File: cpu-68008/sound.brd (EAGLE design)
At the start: 99.7 x 99.7 mm, 36 parts, among them IC101 GAL22V10D, IC102 74HCT175N, IC201 74HC73, IC202 YM3812, IC203 YM3014B, IC204 AY-3-8910, IC301 TL062

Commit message: added analog component to mix on sound card
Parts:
- added C304, C307: 100nF, rcl:C0805
- added C305, C306: 4.7µF, rcl:E2-5
- added IC302: TL062, linear:DIL08
- added R305, R306: 1k, pot:PT-10S
- added R307, R308: 1k, rcl:R2012
- added R309, R310: 4k7, rcl:R2012
- added R311: 10k, pot:PT-10S
- C303: value 100nF -> 220µF; device rcl:C0805 -> rcl:E2,5-6
- moved C303 57.3 mm to (14.0, 91.4), flipped to the top, turned to 90 degrees
- moved R304 15.4 mm to (48.3, 55.2), turned to 0 degrees
- moved R303 15.3 mm to (52.5, 55.2), turned to 0 degrees
- moved R301 12.3 mm to (51.4, 58.4), turned to 90 degrees
- moved R302 12.3 mm to (54.0, 58.4), turned to 90 degrees
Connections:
- new net AUDIO: C303.+, IC302.1, R311.S
- new net N$1: C305.+, R305.S
- new net N$10: C305.-, R307.1
- new net N$11: C306.-, R308.1
- new net N$12: IC302.2, R307.2, R308.2, R311.A
- new net N$13: IC302.6, IC302.7
- new net N$15: IC302.5, R309.2, R310.1
- net +5V: now also C304.1, C307.1, IC302.8, R309.1; no longer C303.1
- net FM_OUT: now also R305.E
- net GND: now also C304.2, C307.2, IC302.3, IC302.4, R305.A, R306.A, R310.2; no longer C303.2
- net N$4: now also C303.-
- net N$7: now also C306.+, R306.S; no longer IC101.7
- net PSG_OUT: now also R306.E
- net SLOT_A0: now also IC101.7
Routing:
- net +5V: track 321.6 -> 379.8 mm, vias 3 -> 4
- net N$12: track 0.00 -> 38.0 mm
- net SLOT_A0: track 59.2 -> 85.9 mm
- net AUDIO: track 0.00 -> 15.7 mm
- net PSG_OUT_C: track 21.5 -> 6.89 mm
- net PSG_OUT: track 7.62 -> 22.0 mm
- net N$15: track 0.00 -> 13.9 mm
- net N$10: track 0.00 -> 9.83 mm
- net N$7: track 0.00 -> 7.87 mm
- net N$1: track 0.00 -> 7.87 mm
- net N$11: track 0.00 -> 6.02 mm
- net N$4: track 0.00 -> 5.50 mm
- net PSG_OUT_A: track 4.87 -> 7.42 mm
- net N$13: track 0.00 -> 2.54 mm
- net PSG_OUT_B: track 4.87 -> 7.30 mm
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
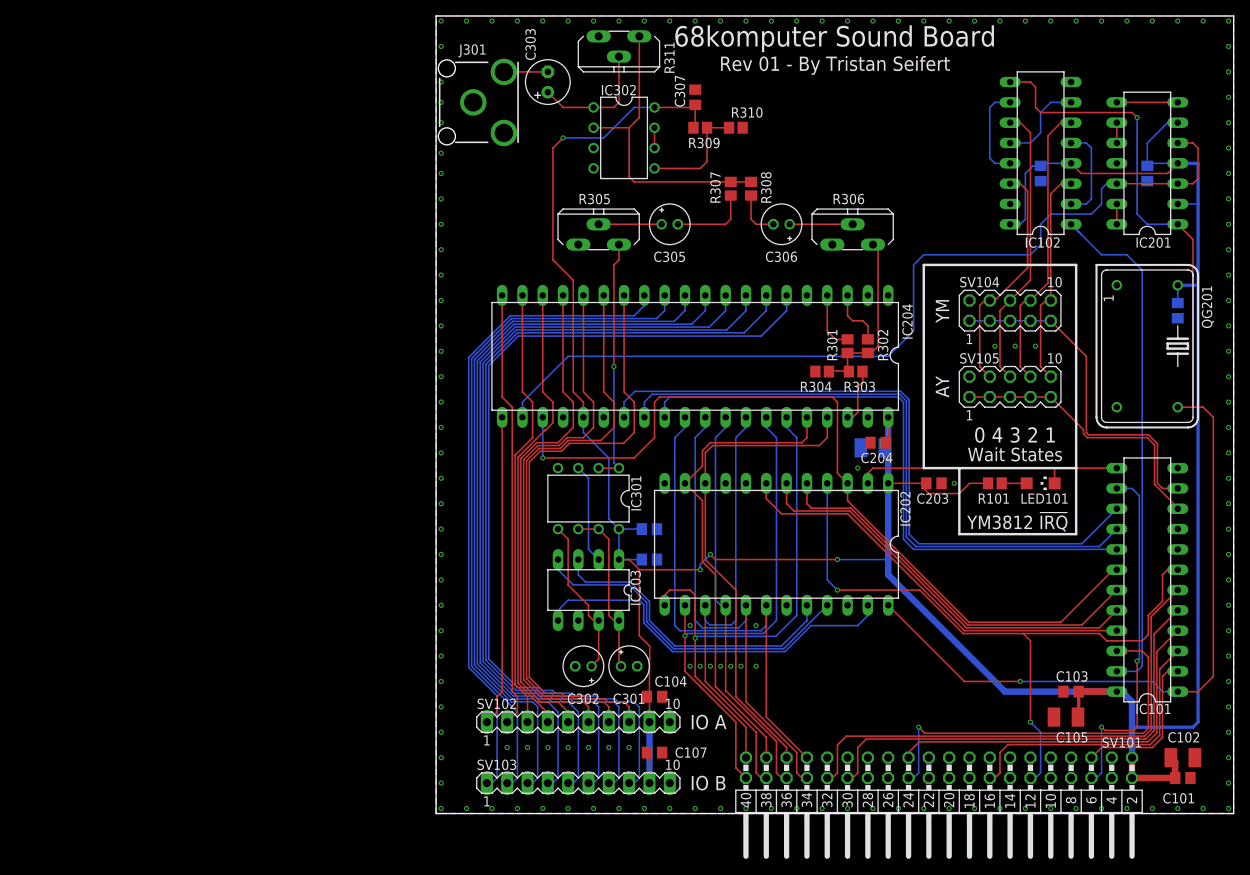
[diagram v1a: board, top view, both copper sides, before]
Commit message: start working on adding midi in/out to sound board
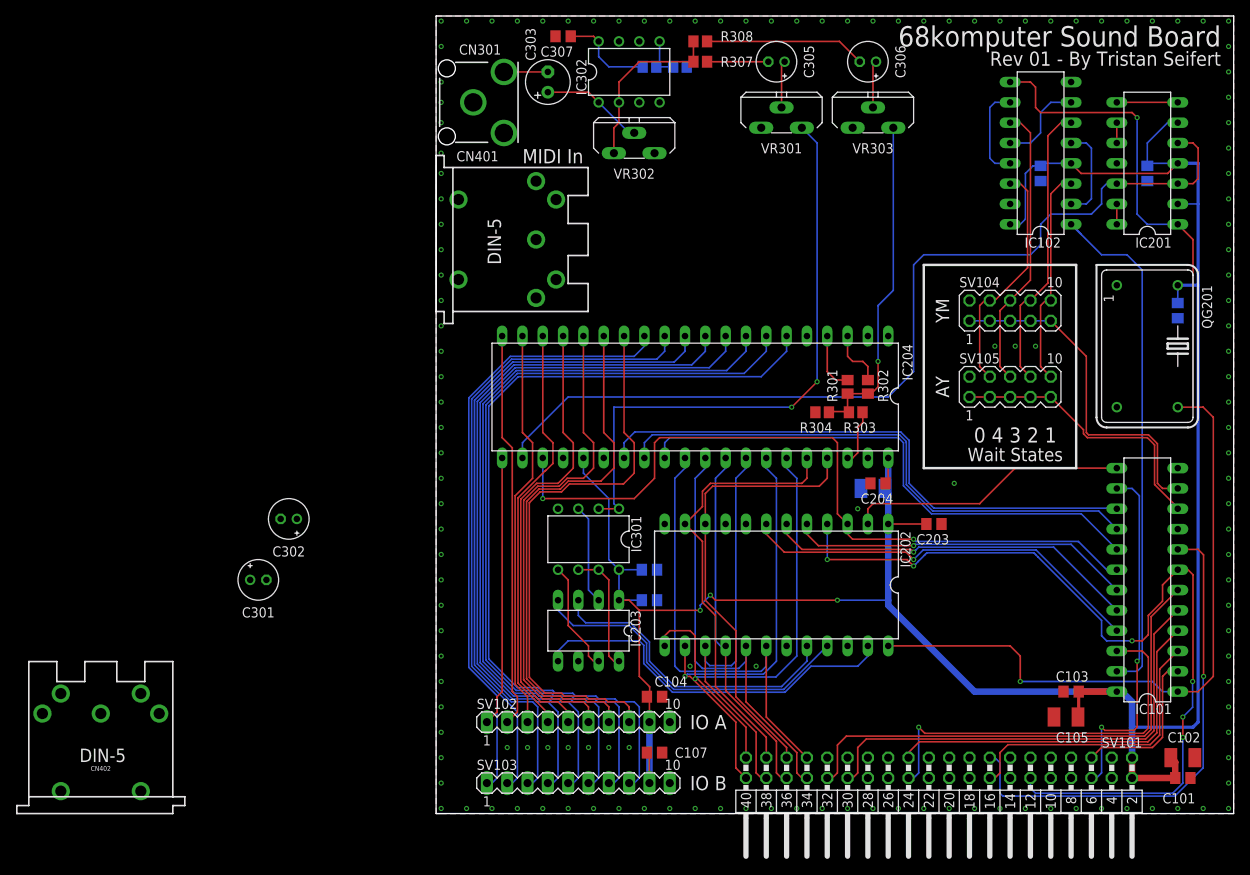
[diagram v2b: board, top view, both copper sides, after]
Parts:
- removed LED101: (no value), led:CHIPLED_1206
- removed R101: 3k, rcl:R2012
- removed R305, R306: 1k, pot:PT-10S
- removed R311: 10k, pot:PT-10S
- added CN401, CN402: DIN5, SparkFun-Connectors:DIN5-RA-PTH
- added VR301, VR303: 1k, pot:PT-10S
- added VR302: 10k, pot:PT-10S
- moved C301 47.6 mm to (-22.2, 29.2)
- moved C302 41.2 mm to (-18.4, 36.8)
- moved C305 24.3 mm to (42.5, 94.0), turned to 180 degrees
- moved C306 23.0 mm to (54.0, 94.0)
- moved R308 19.5 mm to (33.0, 96.5), turned to 180 degrees
- moved C307 18.2 mm to (15.9, 97.2), turned to 180 degrees
- moved R307 16.3 mm to (33.0, 94.0), turned to 180 degrees
- moved R310 10.3 mm to (30.5, 93.3), flipped to the bottom, turned to 180 degrees
- moved R309 9.92 mm to (26.7, 93.3), flipped to the bottom, turned to 180 degrees
- moved IC302 8.28 mm to (24.1, 92.7), turned to 0 degrees
- moved C304 5.08 mm to (26.7, 30.5)
- moved IC202 5.08 mm to (42.5, 28.6)
- moved IC203 5.08 mm to (19.1, 22.9)
- moved C203 5.08 mm to (62.2, 36.2)
- moved C204 5.08 mm to (55.2, 41.3)
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- renumbered J301 to CN301
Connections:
- removed net N$3: LED101.A, R101.2
- removed net N$8: IC101.8
- net !YM_IRQ: no longer LED101.C
- net +5V: no longer R101.1
- net AUDIO: now also VR302.S; no longer R311.S
- net FM_OUT: now also VR301.E; no longer R305.E
- net GND: now also VR301.A, VR303.A; no longer R305.A, R306.A
- net N$1: now also VR301.S; no longer R305.S
- net N$12: now also VR302.A; no longer R311.A
- net N$7: now also VR303.S; no longer R306.S
- net PSG_OUT: now also VR303.E; no longer R306.E
- net SLOT_A9: now also IC101.8
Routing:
- net +5V: track 379.8 -> 316.7 mm, vias 4 -> 3
- net SLOT_A9: track 0.00 -> 62.5 mm, vias 0 -> 1
- net FM_OUT: track 31.0 -> 74.8 mm, vias 1 -> 2
- net SLOT_A0: track 85.9 -> 111.1 mm, vias 2 -> 6
- net PSG_OUT: track 22.0 -> 42.2 mm, vias 0 -> 1
- net N$12: track 38.0 -> 22.1 mm
- net N$11: track 6.02 -> 20.1 mm
- net AY_BDIR: track 83.6 -> 71.2 mm
- net AY_BC2: track 80.1 -> 69.4 mm
- net AY_BC1: track 76.6 -> 67.6 mm
- net N$15: track 13.9 -> 5.28 mm
- net !RESET: track 103.4 -> 95.4 mm, vias 1 -> 2
- net !YM_WR: track 49.4 -> 43.0 mm, vias 0 -> 1
- net YM_OUT_RB: track 20.0 -> 13.9 mm
- net YM_OUT_MP: track 21.2 -> 15.4 mm
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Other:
- board text added: "MIDI In"
- board text removed: "YM3812 !IRQ!"

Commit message: cleaned up routing for sound board a bit, moved some things in preparation of adding midi interface
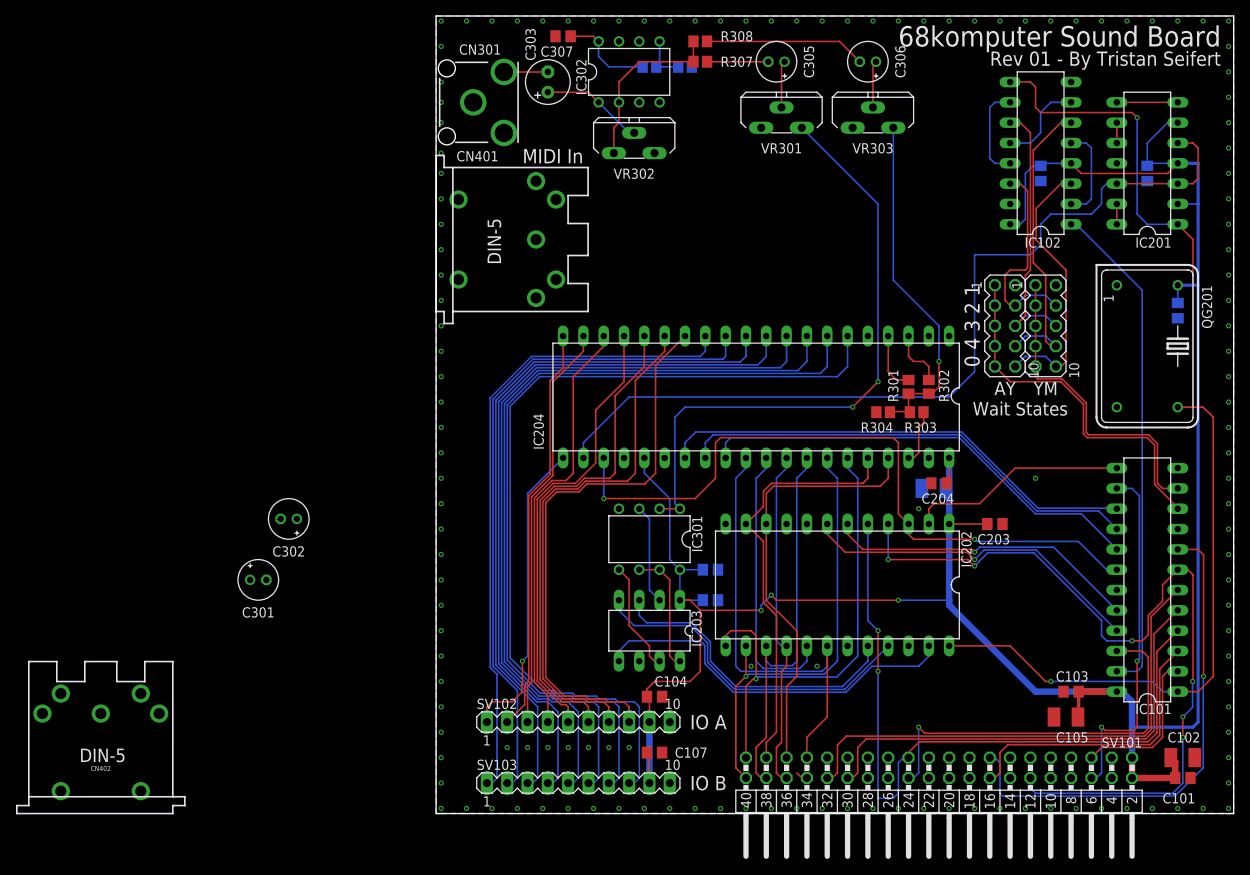
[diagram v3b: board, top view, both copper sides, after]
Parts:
- moved SV105 7.65 mm to (71.1, 61.0), turned to 270 degrees
- moved C204 7.62 mm to (62.9, 41.3)
- moved IC204 7.62 mm to (40.0, 52.1)
- moved R304 7.62 mm to (55.9, 50.2)
- moved IC203 7.62 mm to (26.7, 22.9)
- moved IC301 7.62 mm to (26.7, 34.3)
- moved C203 7.62 mm to (69.8, 36.2)
- moved C205 7.62 mm to (34.3, 26.7)
- moved C206 7.62 mm to (62.2, 40.6)
- moved C304 7.62 mm to (34.3, 30.5)
- moved IC202 7.62 mm to (50.2, 28.6)
- moved R301 7.62 mm to (59.1, 53.3)
- moved R302 7.62 mm to (61.6, 53.3)
- moved R303 7.62 mm to (60.1, 50.2)
- moved SV104 4.84 mm to (76.2, 61.0), turned to 270 degrees
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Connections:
- net !YM_RD renamed !RD
- removed net !YM_WR: IC101.19, IC202.5
- net SLOT_R/!W!: now also IC202.5
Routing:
- net !YM_WR: track 43.0 -> 0.00 mm, vias 1 -> 0
- net SLOT_R/!W!: track 46.6 -> 89.5 mm, vias 0 -> 2
- net SLOT_D6: track 55.0 -> 36.5 mm
- net AY_BC1: track 67.6 -> 56.8 mm
- net AY_BDIR: track 71.2 -> 60.4 mm
- net AY_BC2: track 69.4 -> 58.6 mm
- net !AY_DONE: track 35.1 -> 45.5 mm
- net CLK_A: track 143.5 -> 134.1 mm
- net SLOT_A0: track 111.1 -> 103.5 mm
- net !YM_CS: track 51.1 -> 43.5 mm
- net !RD: track 47.0 -> 39.4 mm
- net !YM_IRQ: track 35.1 -> 27.5 mm
- net !RESET: track 95.4 -> 87.8 mm
- net CLK_B: track 117.1 -> 110.2 mm
- net !DONE_1: track 27.4 -> 34.0 mm
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
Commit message: finished midi circuit frontends
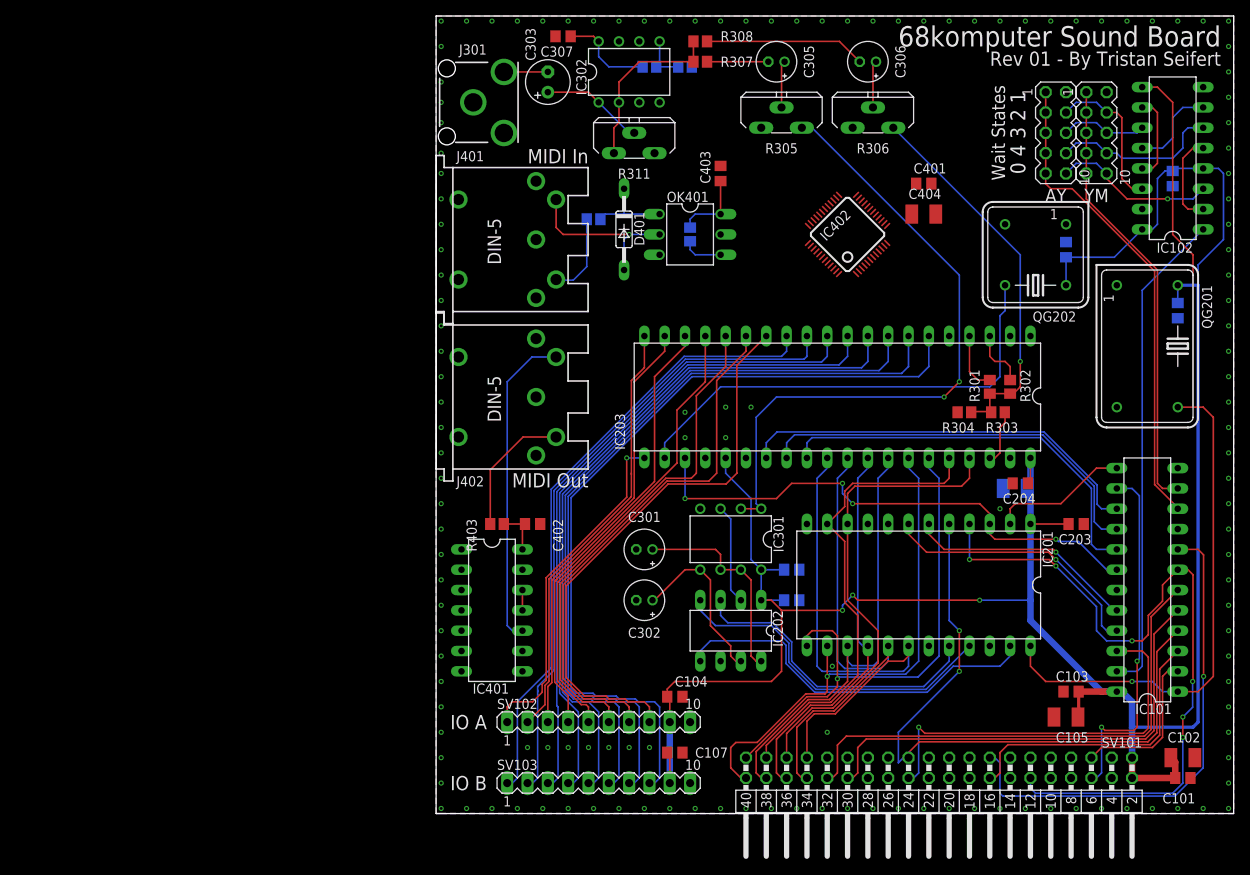
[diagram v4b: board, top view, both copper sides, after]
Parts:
- removed CN402: DIN5, SparkFun-Connectors:DIN5-RA-PTH
- removed IC204: AY-3-8910, 68komputer:DIL40
- added C401, C402, C403: 100nF, rcl:C0805
- added C404: 10µF, rcl:SMC_B
- added D401: 1N914, diode:DO35-10
- added IC401: 74HCT14N, 74xx-eu:DIL14
- added IC402: TL16C550D, 68komputer:LQFP48
- added J402: DIN5, SparkFun-Connectors:DIN5-RA-PTH
- added OK401: H11L1M, optocoupler:DIL06
- added QG202: (no value), crystal:DIL08S
- added R401, R403: 220R, rcl:R2012
- added R402: 4k7, rcl:R2012
- IC201: value 74HC73 -> YM3812; device 74xx-eu:DIL14 -> 68komputer:DIL24
- IC202: value YM3812 -> YM3014B; device 68komputer:DIL24 -> 68komputer:DIL8
- IC203: value YM3014B -> AY-3-8910; device 68komputer:DIL8 -> 68komputer:DIL40
- moved IC201 60.0 mm to (60.3, 28.6), turned to 180 degrees
- moved C301 48.4 mm to (26.0, 33.0), turned to 180 degrees
- moved C302 45.6 mm to (26.0, 26.7)
- moved IC203 37.5 mm to (50.2, 52.1)
- moved SV104 25.0 mm to (82.5, 85.1)
- moved SV105 25.0 mm to (77.5, 85.1)
- moved C106 16.5 mm to (92.1, 79.4)
- moved IC102 16.5 mm to (92.1, 81.9)
- moved IC202 14.5 mm to (36.8, 22.9)
- moved C202 13.9 mm to (78.7, 70.5), turned to 90 degrees
- moved C203 10.2 mm to (80.0, 36.2)
- moved C204 10.2 mm to (73.0, 41.3)
- moved C205 10.2 mm to (44.5, 26.7)
- moved C206 10.2 mm to (72.4, 40.6)
- moved C304 10.2 mm to (44.5, 30.5)
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- renumbered CN301 to J301, CN401 to J401, VR301 to R305, VR302 to R311, VR303 to R306
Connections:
- removed net !CLK_B: IC201.13, IC201.14
- removed net !CLK_C: IC201.7, IC201.8
- removed net CLK_C: IC201.10, IC201.9
- removed net N$9: IC101.9
- new net !MIDI_UART_CS: IC101.19, IC402.11
- new net MIDI_IRQ: IC101.9, IC402.30
- new net MIDI_RESET: IC401.8, IC402.35
- new net MIDI_RX: IC402.7, OK401.4, R402.1
- new net MIDI_RX_+: D401.A, J401.5, OK401.2
- new net MIDI_RX_-: D401.C, OK401.1, R401.2
- new net MIDI_TX: IC401.13, IC402.8
- new net MIDI_TX_-: IC401.10, J402.5
- new net N$14: J401.4, R401.1
- new net N$16: IC401.11, IC401.12
- new net N$17: J402.4, R403.1
- new net N$3: IC402.12, IC402.5
- new net N$8: IC402.10, IC402.9
- new net VCC: IC402.42
- net !RD: now also IC201.6, IC402.19; no longer IC202.6
- net !RESET: now also IC201.3, IC203.23, IC401.9; no longer IC202.3, IC204.23
- net !SLOT_AS: now also IC402.24
- net !YM_CS: now also IC201.7; no longer IC202.7
- net !YM_IRQ: now also IC201.2; no longer IC202.2
- net +5V: now also C401.1, C402.1, C403.1, C404.+, IC201.1, IC203.25, IC203.40, IC401.14, OK401.6, QG202.8, R402.2, R403.2; no longer IC201.2, IC201.4, IC201.6, IC203.1, IC204.25, IC204.40
- net AY_BC1: now also IC203.29; no longer IC204.29
- net AY_BC2: now also IC203.28; no longer IC204.28
- net AY_BDIR: now also IC203.27; no longer IC204.27
- net CLK_A: now also IC201.24; no longer IC201.1, IC202.24
- net CLK_B: now also IC203.22, IC402.14, QG202.5; no longer IC201.12, IC201.3, IC201.5, IC204.22
- net GND: now also C401.2, C402.2, C403.2, C404.-, IC201.12, IC202.6, IC203.1, IC203.24, IC401.1, IC401.3, IC401.5, IC401.7, IC402.18, J402.2, OK401.5, QG202.4; no longer IC201.11, IC202.12, IC203.6, IC204.1, IC204.24
- net IOA0: now also IC203.21; no longer IC204.21
- net IOA1: now also IC203.20; no longer IC204.20
- net IOA2: now also IC203.19; no longer IC204.19
- net IOA3: now also IC203.18; no longer IC204.18
- net IOA4: now also IC203.17; no longer IC204.17
- net IOA5: now also IC203.16; no longer IC204.16
- net IOA6: now also IC203.15; no longer IC204.15
- net IOA7: now also IC203.14; no longer IC204.14
- net IOB0: now also IC203.13; no longer IC204.13
- net IOB1: now also IC203.12; no longer IC204.12
- net IOB2: now also IC203.11; no longer IC204.11
- net IOB3: now also IC203.10; no longer IC204.10
- net IOB4: now also IC203.9; no longer IC204.9
- net IOB5: now also IC203.8; no longer IC204.8
- net IOB6: now also IC203.7; no longer IC204.7
- net IOB7: now also IC203.6; no longer IC204.6
- net PSG_OUT_A: now also IC203.4; no longer IC204.4
- net PSG_OUT_B: now also IC203.3; no longer IC204.3
- net PSG_OUT_C: now also IC203.38; no longer IC204.38
- net SLOT_A0: now also IC201.4, IC402.28; no longer IC202.4
- net SLOT_A1: now also IC402.27
- net SLOT_A2: now also IC402.26
- net SLOT_D0: now also IC201.10, IC203.37, IC402.43; no longer IC202.10, IC204.37
- net SLOT_D1: now also IC201.11, IC203.36, IC402.44; no longer IC202.11, IC204.36
- net SLOT_D2: now also IC201.13, IC203.35, IC402.45; no longer IC202.13, IC204.35
- net SLOT_D3: now also IC201.14, IC203.34, IC402.46; no longer IC202.14, IC204.34
- net SLOT_D4: now also IC201.15, IC203.33, IC402.47; no longer IC202.15, IC204.33
- net SLOT_D5: now also IC201.16, IC203.32, IC402.2; no longer IC202.16, IC204.32
- net SLOT_D6: now also IC201.17, IC203.31, IC402.3; no longer IC202.17, IC204.31
- net SLOT_D7: now also IC201.18, IC203.30, IC402.4; no longer IC202.18, IC204.30
- net SLOT_R/!W!: now also IC201.5, IC402.16; no longer IC202.5
- net YM_DAC_CLK: now also IC201.23, IC202.5; no longer IC202.23, IC203.5
- net YM_DAC_DATA: now also IC201.21, IC202.4; no longer IC202.21, IC203.4
- net YM_DAC_SY: now also IC201.20, IC202.3; no longer IC202.20, IC203.3
- net YM_OUT_BUF: now also IC202.2; no longer IC203.2
- net YM_OUT_MP: now also IC202.8; no longer IC203.8
- net YM_OUT_RB: now also IC202.7; no longer IC203.7
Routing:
- net CLK_B: track 110.2 -> 58.9 mm
- net MIDI_TX_-: track 0.00 -> 40.0 mm
- net CLK_A: track 134.1 -> 108.6 mm, vias 2 -> 1
- net !DONE_3: track 34.1 -> 10.8 mm
- net SLOT_D6: track 36.5 -> 58.6 mm
- net MIDI_RX_+: track 0.00 -> 21.5 mm, vias 0 -> 1
- net !RESET: track 87.8 -> 66.5 mm, vias 2 -> 4
- net !DONE_2: track 38.3 -> 21.2 mm
- net N$17: track 0.00 -> 16.7 mm
- net !YM_DONE: track 40.0 -> 55.4 mm
- net !AY_DONE: track 45.5 -> 60.5 mm
- net !DONE_1: track 34.0 -> 20.4 mm, vias 0 -> 1
- net SLOT_A0: track 103.5 -> 92.6 mm
- net MIDI_RX_-: track 0.00 -> 10.8 mm
- net YM_OUT_MP: track 15.4 -> 26.1 mm
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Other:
- board text added: "MIDI Out"
